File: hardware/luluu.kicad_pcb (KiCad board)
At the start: 2 copper layers, 75 x 30 mm, 53 parts, among them J1 BATT_CON, J2 RPi SWD, J3 STEMMA_{QT} I_{2}C, J4 Micro_SD_Card, J5 RPi UART, J6 USB_C_Receptacle_USB2.0, J7 DISP_LCD_ST7789, Q1 AO3401A, Q2 BSS138, SW1 SW_USBBOOT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

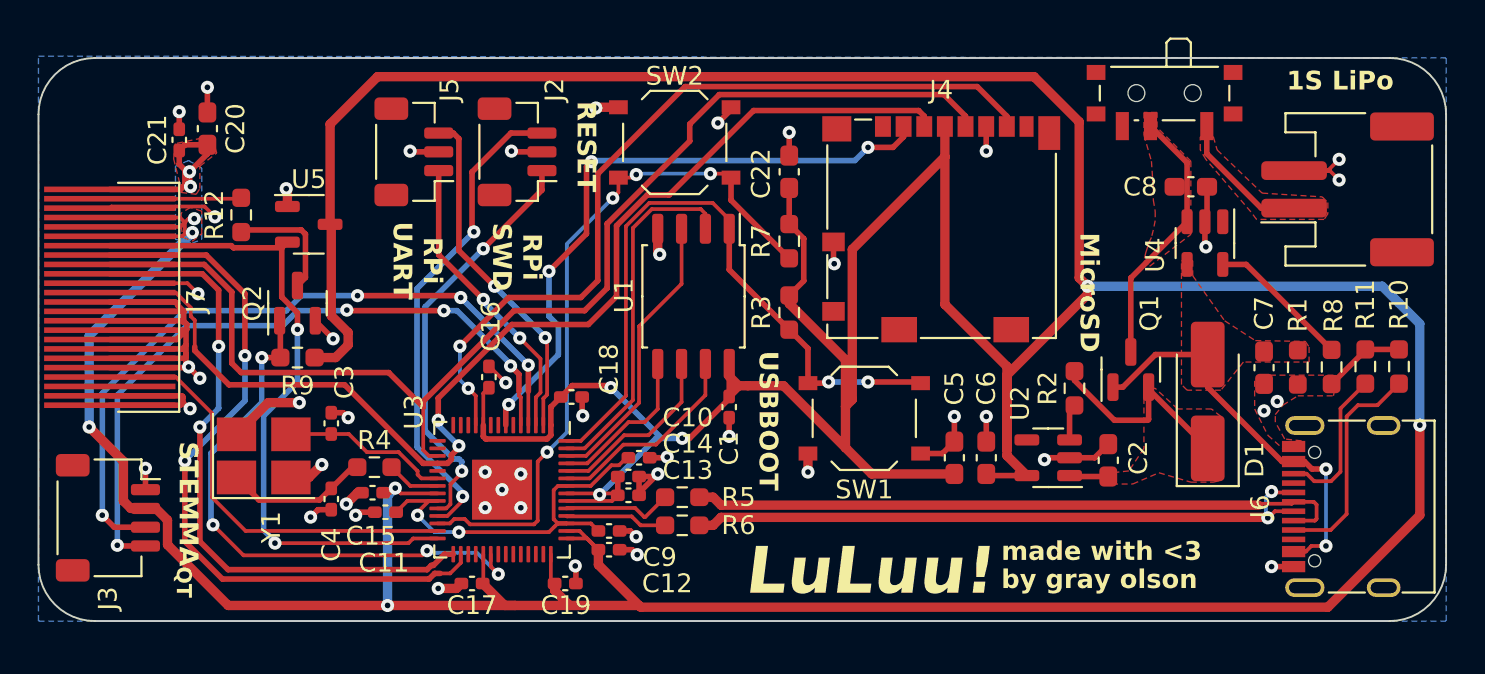
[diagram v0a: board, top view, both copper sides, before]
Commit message: update pwr switch silkscreen
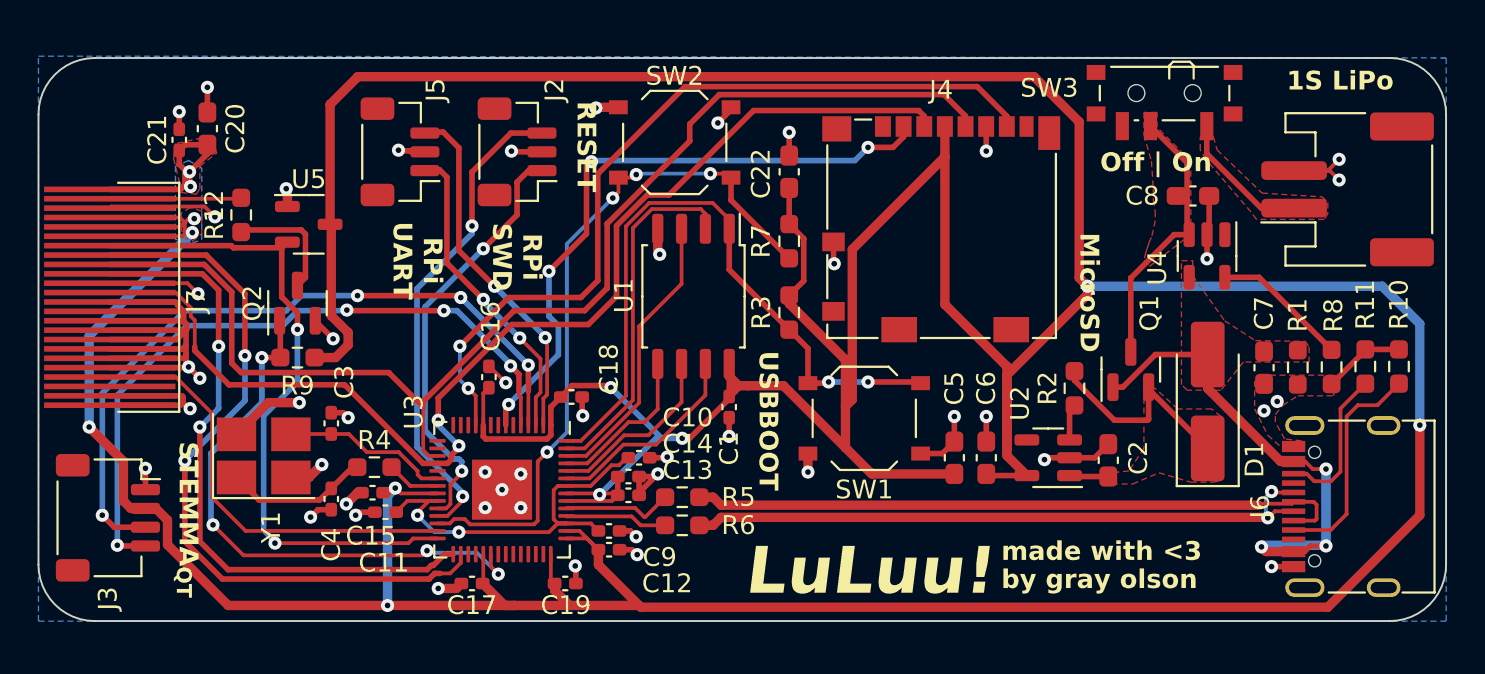
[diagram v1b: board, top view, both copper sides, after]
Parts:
- SW3: footprint Button_Switch_SMD:SW_SPDT_PCM12 -> luluu:SW_SPDT_PCM12
- moved J5 0.74 mm to (131.5, 83.2)
- moved U4 0.70 mm to (174.5, 88.8)
- moved C8 0.50 mm to (173.8, 85.6)
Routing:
- net +5V: track 21.6 -> 26.9 mm, vias 2 -> 3
- net UART_{RX}: track 15.9 -> 16.7 mm
- net +3V3: track 348.7 -> 349.3 mm
- net +BATT: track 14.1 -> 14.6 mm
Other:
- board text added: "Off | On"
